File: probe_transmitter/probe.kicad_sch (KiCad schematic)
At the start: 18 parts, among them Q1 PMST2222, U1 ATtiny85-20M

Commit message: - add fix for PCB v1.1 (fix resistor place 1608)
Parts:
- R1, R2, R3, R4, R5, R6, R7: footprint Resistor_SMD:R_0201_0603Metric_Pad0.64x0.40mm_HandSolder -> Resistor_SMD:R_0603_1608Metric
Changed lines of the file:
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@@
     (property "Reference" "R4" (id 0) (at 146.05 68.58 90))
     (property "Value" "R39" (id 1) (at 146.05 71.12 90))
-    (property "Footprint" "Resistor_SMD:R_0201_0603Metric_Pad0.64x0.40mm_HandSolder" (id 2) (at 146.05 76.708 90)
+    (property "Footprint" "Resistor_SMD:R_0603_1608Metric" (id 2) (at 146.05 76.708 90)
       (effects (font (size 1.27 1.27)) hide)
     )
@@
     (property "Reference" "R6" (id 0) (at 92.71 66.04 90))
     (property "Value" "R39" (id 1) (at 92.71 68.58 90))
-    (property "Footprint" "Resistor_SMD:R_0201_0603Metric_Pad0.64x0.40mm_HandSolder" (id 2) (at 92.71 74.168 90)
+    (property "Footprint" "Resistor_SMD:R_0603_1608Metric" (id 2) (at 92.71 74.168 90)
       (effects (font (size 1.27 1.27)) hide)
     )
@@
       (effects (font (size 1.27 1.27)) (justify right))
     )
-    (property "Footprint" "Resistor_SMD:R_0201_0603Metric_Pad0.64x0.40mm_HandSolder" (id 2) (at 67.818 86.36 90)
+    (property "Footprint" "Resistor_SMD:R_0603_1608Metric" (id 2) (at 67.818 86.36 90)
       (effects (font (size 1.27 1.27)) hide)
     )
@@
     (property "Reference" "R3" (id 0) (at 146.05 58.42 90))
     (property "Value" "R39" (id 1) (at 146.05 60.96 90))
-    (property "Footprint" "Resistor_SMD:R_0201_0603Metric_Pad0.64x0.40mm_HandSolder" (id 2) (at 146.05 66.548 90)
+    (property "Footprint" "Resistor_SMD:R_0603_1608Metric" (id 2) (at 146.05 66.548 90)
       (effects (font (size 1.27 1.27)) hide)
     )
@@
     (property "Reference" "R1" (id 0) (at 90.17 55.88 90))
     (property "Value" "R39" (id 1) (at 90.17 58.42 90))
-    (property "Footprint" "Resistor_SMD:R_0201_0603Metric_Pad0.64x0.40mm_HandSolder" (id 2) (at 90.17 64.008 90)
+    (property "Footprint" "Resistor_SMD:R_0603_1608Metric" (id 2) (at 90.17 64.008 90)
       (effects (font (size 1.27 1.27)) hide)
     )
@@
     (property "Reference" "R2" (id 0) (at 146.05 48.26 90))
     (property "Value" "R39" (id 1) (at 146.05 50.8 90))
-    (property "Footprint" "Resistor_SMD:R_0201_0603Metric_Pad0.64x0.40mm_HandSolder" (id 2) (at 146.05 56.388 90)
+    (property "Footprint" "Resistor_SMD:R_0603_1608Metric" (id 2) (at 146.05 56.388 90)
       (effects (font (size 1.27 1.27)) hide)
     )
@@
     (property "Reference" "R5" (id 0) (at 127 31.75 90))
     (property "Value" "R39" (id 1) (at 127 34.29 90))
-    (property "Footprint" "Resistor_SMD:R_0201_0603Metric_Pad0.64x0.40mm_HandSolder" (id 2) (at 127 39.878 90)
+    (property "Footprint" "Resistor_SMD:R_0603_1608Metric" (id 2) (at 127 39.878 90)
       (effects (font (size 1.27 1.27)) hide)
     )
@@
     )
     (path "/c9f85c58-8dc9-4813-a0a9-a0d629eb5414"
-      (reference "R1") (unit 1) (value "R39") (footprint "Resistor_SMD:R_0201_0603Metric_Pad0.64x0.40mm_HandSolder")
+      (reference "R1") (unit 1) (value "R39") (footprint "Resistor_SMD:R_0603_1608Metric")
     )
     (path "/d1045195-de6f-4f74-9a2f-7fefb8161a3f"
-      (reference "R2") (unit 1) (value "R39") (footprint "Resistor_SMD:R_0201_0603Metric_Pad0.64x0.40mm_HandSolder")
+      (reference "R2") (unit 1) (value "R39") (footprint "Resistor_SMD:R_0603_1608Metric")
     )
     (path "/71fdf9b5-9e65-42fe-b540-7524bcd9e0d5"
-      (reference "R3") (unit 1) (value "R39") (footprint "Resistor_SMD:R_0201_0603Metric_Pad0.64x0.40mm_HandSolder")
+      (reference "R3") (unit 1) (value "R39") (footprint "Resistor_SMD:R_0603_1608Metric")
     )
     (path "/0188f7fb-ebbb-4b52-979b-808f2b56eeab"
-      (reference "R4") (unit 1) (value "R39") (footprint "Resistor_SMD:R_0201_0603Metric_Pad0.64x0.40mm_HandSolder")
+      (reference "R4") (unit 1) (value "R39") (footprint "Resistor_SMD:R_0603_1608Metric")
     )
     (path "/fea158f0-aae6-4440-99ac-d02a06b99286"
-      (reference "R5") (unit 1) (value "R39") (footprint "Resistor_SMD:R_0201_0603Metric_Pad0.64x0.40mm_HandSolder")
+      (reference "R5") (unit 1) (value "R39") (footprint "Resistor_SMD:R_0603_1608Metric")
     )
     (path "/049afad4-9258-40d9-bd9f-d2d3b25bdb71"
-      (reference "R6") (unit 1) (value "R39") (footprint "Resistor_SMD:R_0201_0603Metric_Pad0.64x0.40mm_HandSolder")
+      (reference "R6") (unit 1) (value "R39") (footprint "Resistor_SMD:R_0603_1608Metric")
     )
     (path "/63b532ea-928c-43d9-bde5-0db28ffe2de6"
-      (reference "R7") (unit 1) (value "R10M") (footprint "Resistor_SMD:R_0201_0603Metric_Pad0.64x0.40mm_HandSolder")
+      (reference "R7") (unit 1) (value "R10M") (footprint "Resistor_SMD:R_0603_1608Metric")
     )
     (path "/5a62b5e6-9018-4528-a2eb-c56da5886269"

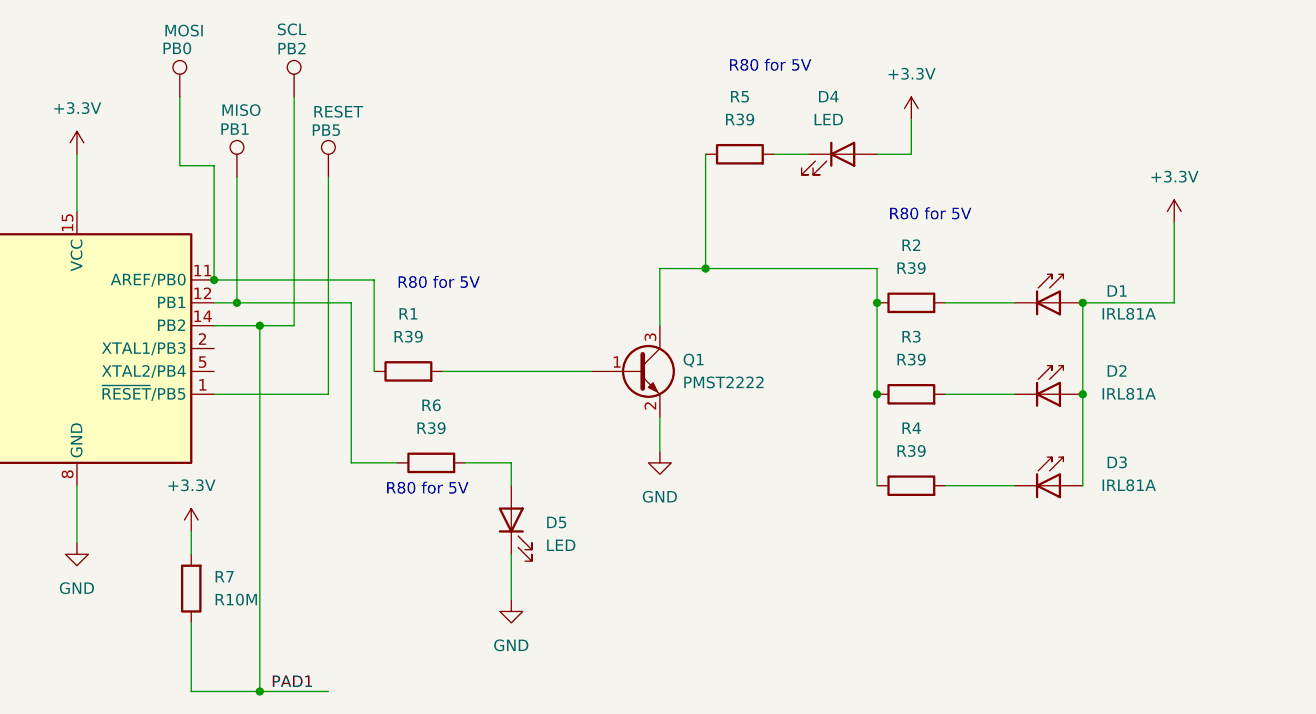
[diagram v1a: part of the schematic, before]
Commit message: - update probe transmitter
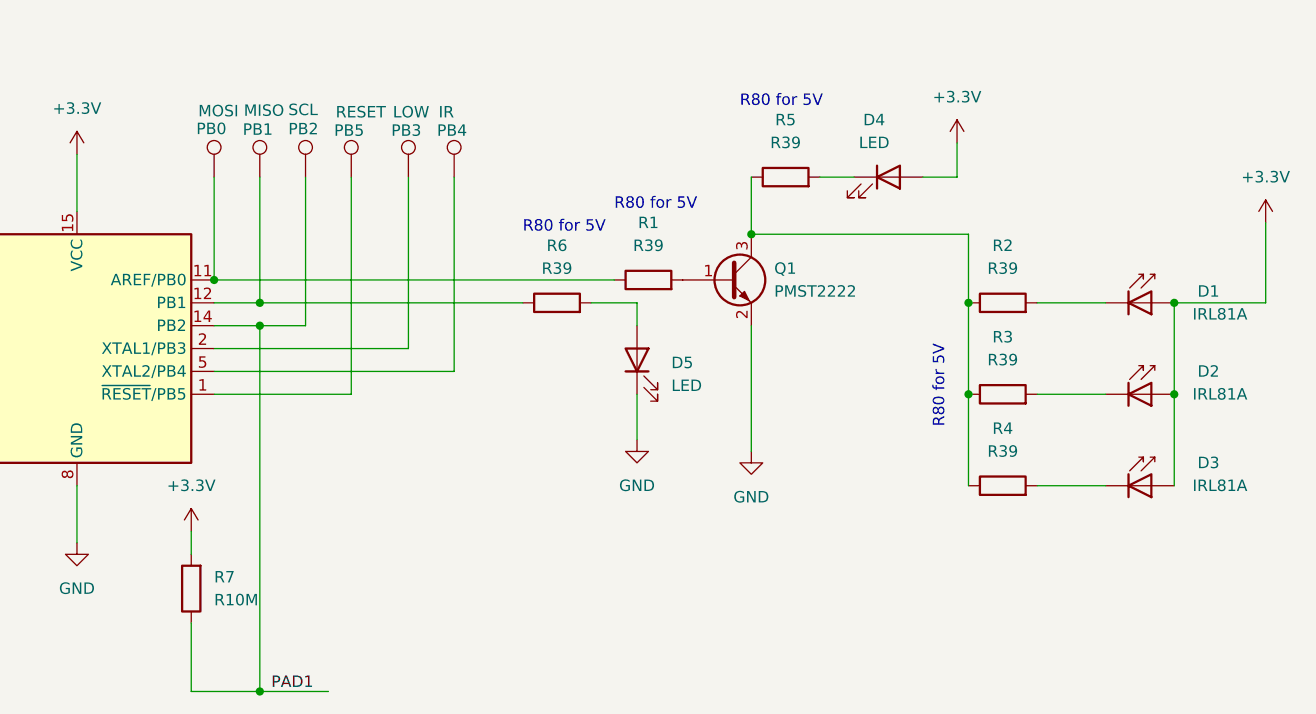
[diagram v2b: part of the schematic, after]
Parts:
- added IR: PB4, TestPoint:TestPoint_Pad_D1.0mm, symbol Connector:TestPoint
- added LOW: PB3, TestPoint:TestPoint_Pad_D1.0mm, symbol Connector:TestPoint
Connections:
- net at U1.2 (XTAL1/PB3): now also LOW.1
- net at U1.5 (XTAL2/PB4): now also IR.1
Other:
- moved on the sheet: D1, D2, D3, D4, D5, MISO, MOSI, Q1, R1, R2, R3, R4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

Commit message: - add new power version
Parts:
- removed D1, D2, D3: IRL81A, LED_THT:LED_SideEmitter_Rectangular_W4.5mm_H1.6mm, symbol LED:IRL81A
- removed R3, R4: R39, Resistor_SMD:R_0603_1608Metric, symbol Device:R
- added IR_LED1: PB4, TestPoint:TestPoint_Pad_D1.0mm, symbol Connector:TestPoint
- added Q2: PMST2222, Package_TO_SOT_SMD:SOT-23, symbol Transistor_BJT:BC817
- renumbered IR to IR1, LOW to LOW1, MISO to MISO1, MOSI to MOSI1, RESET to RESET1, SCL to SCL1
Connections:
- net GND: now also Q2.2 (E)
- net at Q1.3 (C), R5.1: now also IR_LED1.1; no longer R2.1
- net at U1.5 (XTAL2/PB4): now also R2.1; no longer IR1.1
- net at R2.2: now also Q2.1 (B)
- new net: IR1.1, Q2.3 (C)
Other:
- moved on the sheet: D5, IR1, R6

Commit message: -add new version for transmitter
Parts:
- removed IR1, IR_LED1: PB4, TestPoint:TestPoint_Pad_D1.0mm, symbol Connector:TestPoint
- removed LOW1: PB3, TestPoint:TestPoint_Pad_D1.0mm, symbol Connector:TestPoint
- removed U1: ATtiny85-20M, Package_DFN_QFN:QFN-20-1EP_4x4mm_P0.5mm_EP2.6x2.6mm, symbol MCU_Microchip_ATtiny:ATtiny85-20M
- added J2: Conn_01x06, Connector_FFC-FPC:TE_0-1734839-6_1x06-1MP_P0.5mm_Horizontal, symbol Connector_Generic:Conn_01x06
- added U2: ATtiny84-20M, Package_DFN_QFN:QFN-20-1EP_4x4mm_P0.5mm_EP2.6x2.6mm, symbol MCU_Microchip_ATtiny:ATtiny84-20M
- renumbered RESET1 to RES1
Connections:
- net +3.3V: now also J2.1 (Pin_1), U2.9 (VCC)
- net GND: now also J2.6 (Pin_6), U2.21 (GND), U2.8 (GND)
- net PAD1: now also U2.14 (PB2); no longer SCL1.1
- net at R6.1: now also U2.12 (XTAL2/PB1); no longer MISO1.1
- net at MOSI1.1: now also U2.16 (PA6); no longer R1.1
- net at Q1.3 (C), R5.1: now also J2.2 (Pin_2)
- net at RES1.1: now also U2.13 (~{RESET}/PB3)
- net at R2.1: now also U2.2 (PA3)
- net at Q2.3 (C): now also J2.3 (Pin_3)
- new net: SCL1.1, U2.1 (PA4)
- new net: R1.1, U2.11 (XTAL1/PB0)
- new net: J2.5 (Pin_5), U2.15 (PA7)
- new net: MISO1.1, U2.20 (PA5)
- new net: J2.4 (Pin_4), U2.3 (PA2)
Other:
- moved on the sheet: D4, D5, MISO1, MOSI1, Q1, Q2, R1, R2, R5, R6, R7, RES1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
